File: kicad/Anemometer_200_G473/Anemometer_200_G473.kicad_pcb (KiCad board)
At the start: 2 copper layers, 23.3 x 37.9 mm, 81 parts, among them J1 Conn_01x01_Female, J10 Conn_01x01_Female, J11 USB_B_Micro, J12 Conn_01x01_Female, J13 Conn_01x01_Female, J14 Conn_01x01_Female, J15 Conn_01x01_Female, J16 Conn_01x01_Female, J17 Conn_01x01_Female, J18 Conn_01x01_Female, J2 Conn_01x01_Female, J20 Conn_01x01_Female, J21 Conn_01x01_Female, J22 Conn_01x01_Female, J3 Conn_01x08_Shielded, J9 Conn_01x01_Female, U1 W5500, U2 NCP1117-3.3, Y1 16, Y2 Crystal_GND24_Small

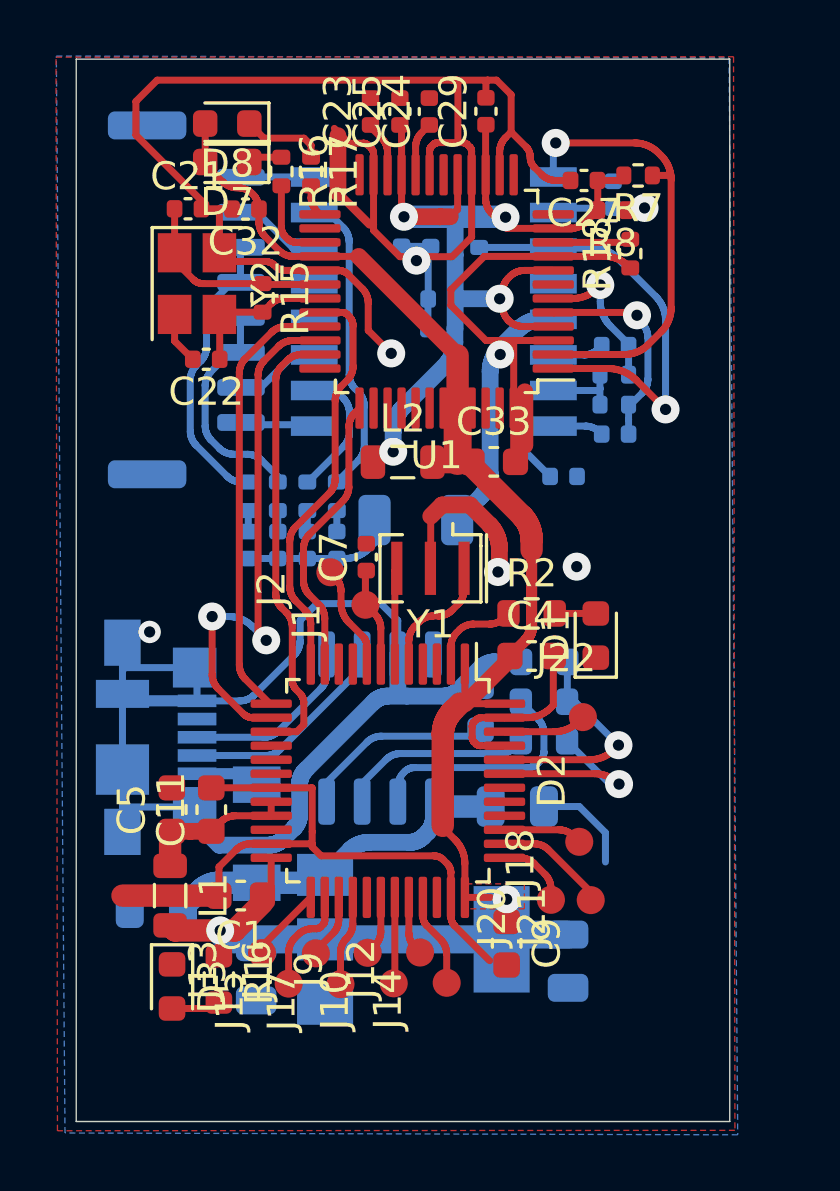
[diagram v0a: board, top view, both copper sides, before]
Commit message: изменено:      kicad/Anemometer_200_G473/Anemometer_200_G473-cache.lib 	изменено:      kicad/Anemometer_200_G473/Anemometer_200_G473.kicad_pcb 	изменено:      kicad/Anemometer_200_G473/Anemometer_200_G473.kicad_pcb-bak 	изменено:      kicad/Anemometer_200_G473/Anemometer_200_G473.sch 	изменено:      kicad/Anemometer_200_G473/Anemometer_200_G473.sch-bak 	изменено:      kicad/Anemometer_200_G473/sym-lib-table 	изменено:      stm32cubeide/Anemometer_G474CBT6_MATLAB/Anemometer_G473CBT7_MATLAB.ioc 	изменено:      stm32cubeide/Anemometer_G474CBT6_MATLAB/Core/Inc/main.h 	изменено:      stm32cubeide/Anemometer_G474CBT6_MATLAB/Core/Src/main.c 	изменено:      stm32cubeide/Anemometer_G474CBT6_MATLAB/Release/Anemometer_G473CBT7_MATLAB.elf 	изменено:      stm32cubeide/Anemometer_G474CBT6_MATLAB/Release/Anemometer_G473CBT7_MATLAB.list 	изменено:      stm32cubeide/Anemometer_G474CBT6_MATLAB/Release/Anemometer_G473CBT7_MATLAB.map 	изменено:      stm32cubeide/Anemometer_G474CBT6_MATLAB/Release/Core/Src/main.cyclo 	изменено:      stm32cubeide/Anemometer_G474CBT6_MATLAB/Release/Core/Src/main.o 	изменено:      stm32cubeide/Anemometer_G474CBT6_MATLAB/Release/Core/Src/main.su
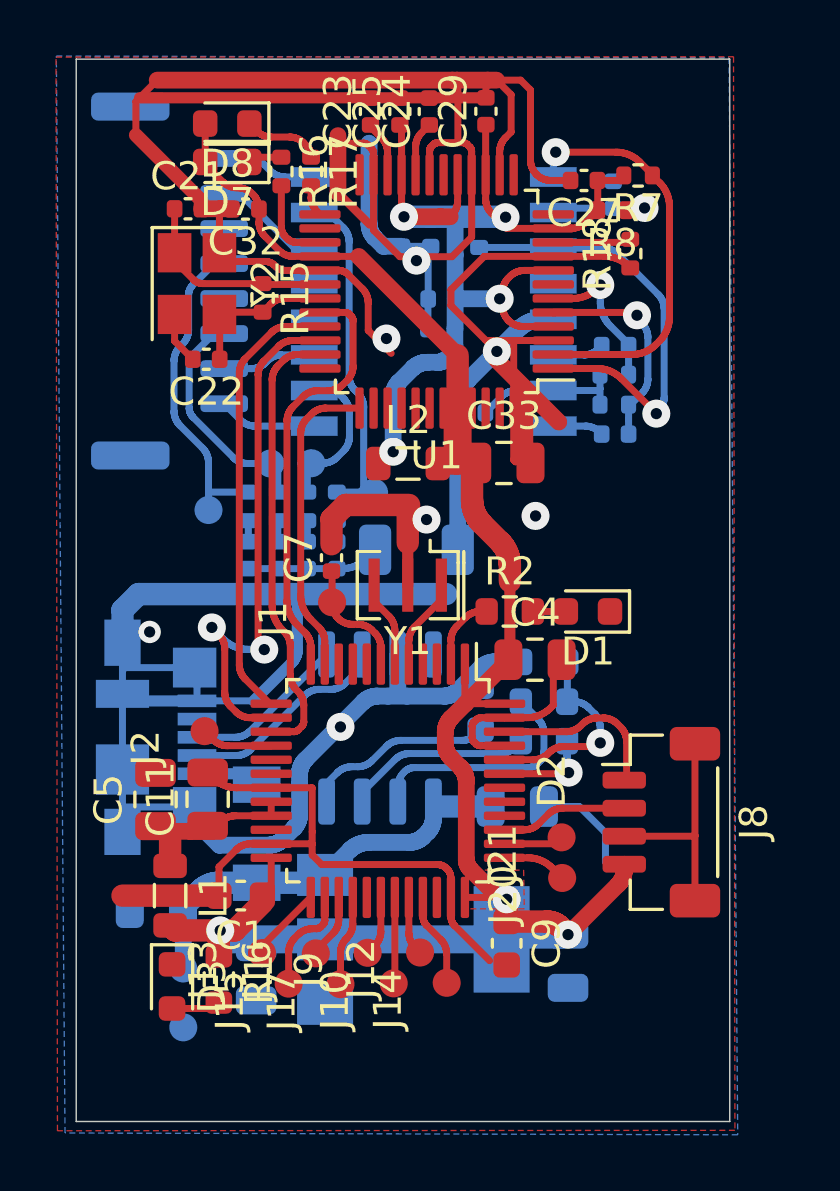
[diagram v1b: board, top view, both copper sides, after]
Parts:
- removed J22: Conn_01x01_Female, My-library:mini_conn
- added J19: Conn_01x01_Female, My-library:mini_conn, B.Cu at (21.0, 64.7)
- added J4: Conn_01x01_Female, My-library:mini_conn, B.Cu at (25.6, 44.6)
- added J5: Conn_01x01_Female, My-library:mini_conn, B.Cu at (27.8, 45.6)
- added J6: Conn_01x01_Female, My-library:mini_conn, B.Cu at (21.9, 46.2)
- added J7: Conn_01x01_Female, My-library:mini_conn, B.Cu at (24.1, 44.6)
- added J8: Conn_01x04_Shielded, Connector_JST:JST_SH_BM04B-SRSS-TB_1x04-1MP_P1.00mm_Vertical, F.Cu at (38.1, 57.4)
- C11, C33, C4, C5: footprint Capacitor_SMD:C_0603_1608Metric -> Capacitor_SMD:C_0805_2012Metric
- J18: moved to B.Cu
- moved J18 14.8 mm to (21.0, 62.6), turned to 0 degrees
- moved J2 7.23 mm to (21.8, 54.1)
- moved C19 3.98 mm to (31.3, 42.8), turned to 180 degrees
- moved J21 2.47 mm to (34.5, 57.9)
- moved C7 1.24 mm to (26.3, 48.0)
- moved J1 1.19 mm to (26.3, 49.5)
- moved C20 1.06 mm to (29.3, 47.7)
- moved Y1 1.01 mm to (29.0, 48.9)
- moved D1 0.90 mm to (35.5, 49.9), turned to 180 degrees
- moved J3 0.90 mm to (20.5, 38.1)
- moved J20 0.88 mm to (34.5, 59.4)
- moved R2 0.78 mm to (32.7, 49.9)
- moved C5 0.68 mm to (20.0, 56.6)
- moved C11 0.39 mm to (21.9, 56.6)
- moved C33 0.36 mm to (32.5, 44.6)
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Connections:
- net Net-(D6-Pad10) renamed /V1
- net Net-(D6-Pad15) renamed /V2
- net Net-(J3-Pad3) renamed /V3
- net Net-(J3-Pad5) renamed /V4
- C10 pad 1: Net-(C10-Pad1) -> /+5v
- C12 pad 1: Net-(C10-Pad1) -> /+5v
- D2 pad 16: (no net) -> /AIn
- D2 pad 39: /scl -> scl
- D2 pad 46: /sda -> sda
- D2 pad 8: /AIn -> (no net)
- D4 pad 1: Net-(C10-Pad1) -> /+5v
- D5 pad 5: Net-(C10-Pad1) -> /+5v
- J18 pad 1: /scl -> /+5v
- U2 pad 3: Net-(C10-Pad1) -> /+5v
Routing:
- net GND: track 173.5 -> 215.5 mm, vias 6 -> 7
- net /+5v: track 0.00 -> 15.2 mm
- net Net-(C10-Pad1): track 13.0 -> 0.00 mm
- net sda: track 0.00 -> 6.37 mm
- net +3V3: track 62.1 -> 66.9 mm, vias 2 -> 3
- net scl: track 0.00 -> 4.53 mm
- net /sda: track 2.96 -> 0.00 mm
- net /scl: track 2.81 -> 0.00 mm
- net Net-(D2-Pad43): track 6.68 -> 3.98 mm
- net /V3: track 10.3 -> 12.8 mm
- net /swc: track 4.05 -> 2.13 mm
- net Net-(C19-Pad1): track 7.32 -> 5.49 mm
- net Net-(D6-Pad1): track 16.4 -> 14.8 mm
- net /V2: track 10.9 -> 12.3 mm
- net /V4: track 8.18 -> 9.52 mm
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
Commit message: изменено:      kicad/Anemometer_200_G473/Anemometer_200_G473-cache.lib 	изменено:      kicad/Anemometer_200_G473/Anemometer_200_G473.kicad_pcb 	изменено:      kicad/Anemometer_200_G473/Anemometer_200_G473.kicad_pcb-bak 	изменено:      kicad/Anemometer_200_G473/Anemometer_200_G473.sch 	изменено:      kicad/Anemometer_200_G473/Anemometer_200_G473.sch-bak
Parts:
- moved R5 4.34 mm to (33.9, 56.0)
- moved C8 2.80 mm to (33.9, 51.7), turned to 0 degrees
- moved R4 1.57 mm to (33.9, 54.7)
- moved C12 1.54 mm to (33.8, 58.1)
- moved R3 1.28 mm to (33.9, 53.2)
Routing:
- net GND: track 215.5 -> 209.7 mm
- net Net-(D2-Pad44): track 7.37 -> 3.64 mm
- net Net-(C8-Pad1): track 6.82 -> 9.87 mm
- net Net-(D5-Pad6): track 8.55 -> 5.62 mm
- net Net-(D2-Pad43): track 3.98 -> 6.72 mm
- net /+5v: track 15.2 -> 16.4 mm
- net Net-(D5-Pad7): track 6.68 -> 7.89 mm

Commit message: изменено:      kicad/Anemometer_200_G473/Anemometer_200_G473.kicad_pcb 	изменено:      kicad/Anemometer_200_G473/Anemometer_200_G473.kicad_sch
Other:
- net class Default removed

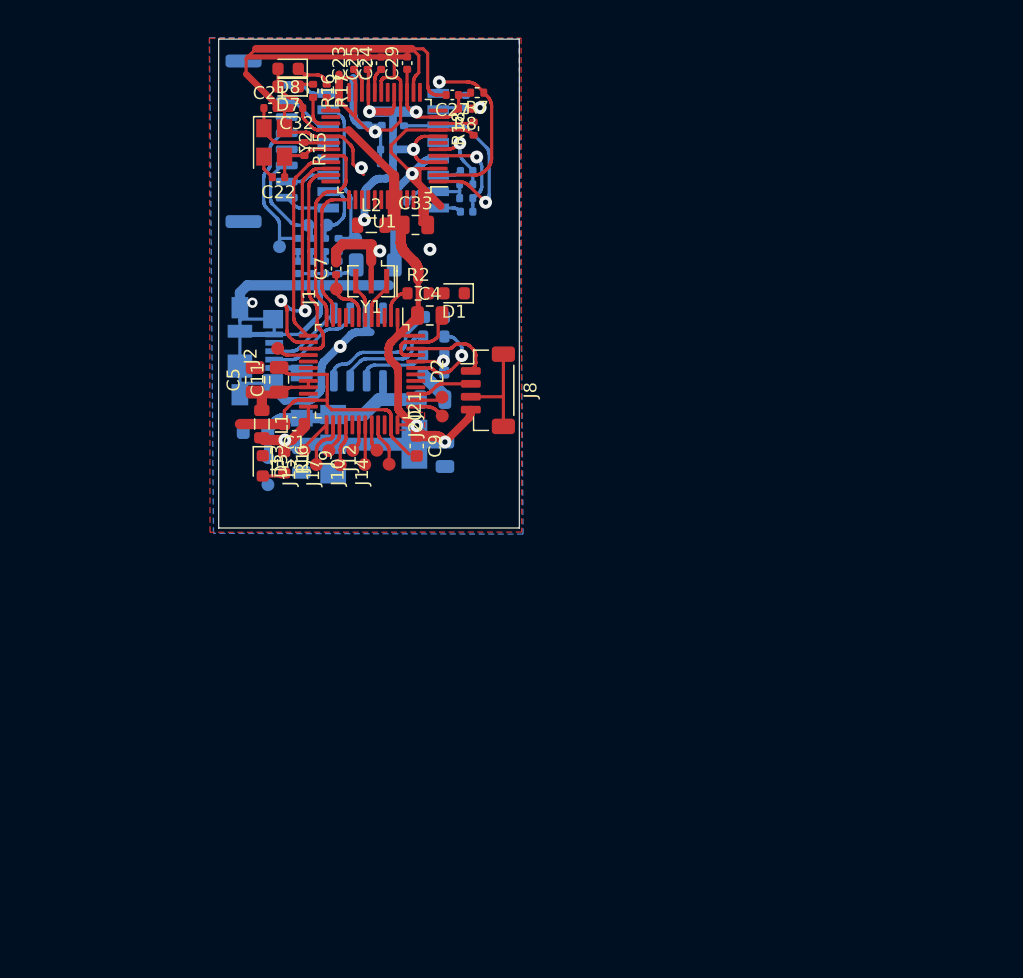
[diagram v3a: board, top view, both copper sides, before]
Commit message: изменено:      kicad/Amp200_2/Amp200-rescue.lib 	изменено:      kicad/Anemometer_200_G473/Anemometer_200_G473.kicad_pcb 	изменено:      kicad/Anemometer_200_G473/Anemometer_200_G473.kicad_prl 	изменено:      kicad/Anemometer_200_G473/Anemometer_200_G473.kicad_sch 	изменено:      kicad/Anemometer_200_G473/fp-info-cache 	изменено:      kicad/Anemometr_v3/Anemometr-rescue.lib
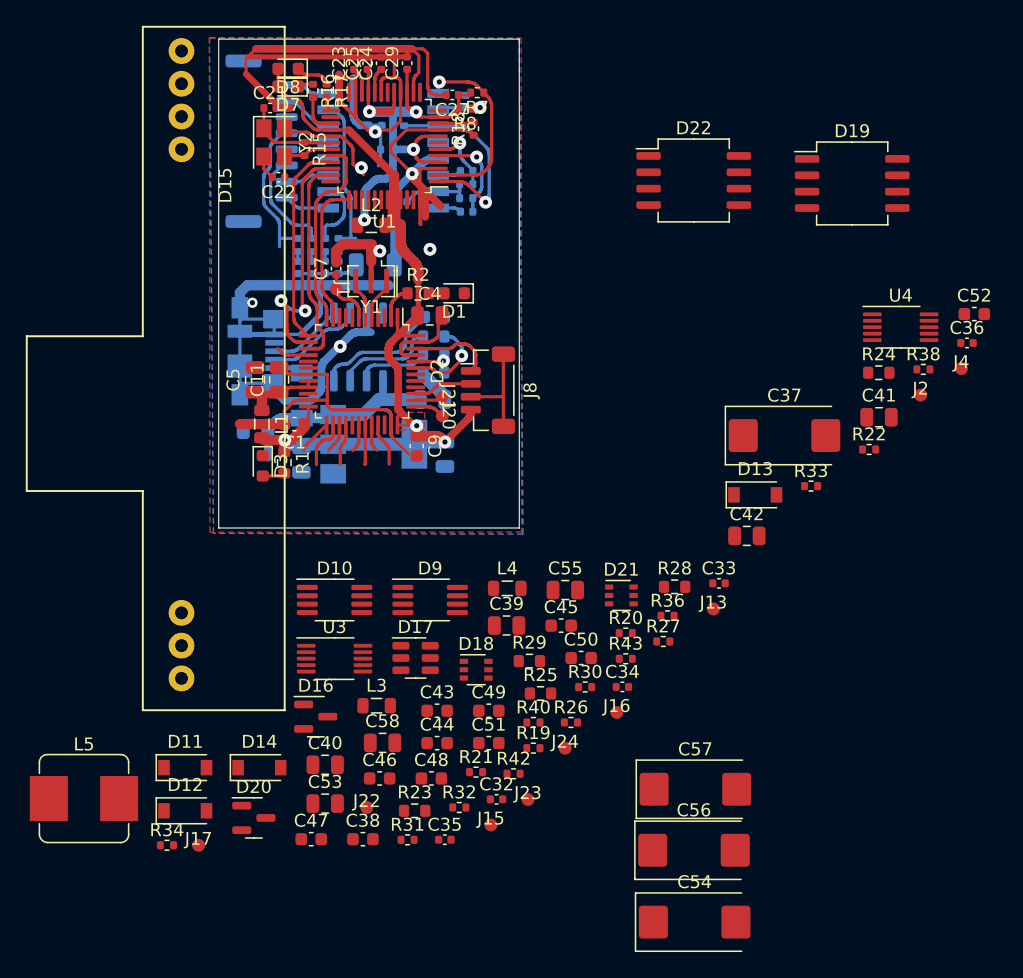
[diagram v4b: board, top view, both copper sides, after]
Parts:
- removed J10, J12, J14, J18, J19, J5, J6, J7, J9: Conn_01x01_Female, My-library:mini_conn
- added C34: 4.7u, Capacitor_SMD:C_0402_1005Metric, F.Cu at (48.5, 80.4)
- added C35: 4.7u, Capacitor_SMD:C_0402_1005Metric, F.Cu at (34.7, 92.2)
- added C36: 6.8n, Capacitor_SMD:C_0402_1005Metric, F.Cu at (75.2, 53.7)
- added C37: CP, Capacitor_Tantalum_SMD:CP_EIA-7343-40_Kemet-Y_Pad2.25x2.55mm_HandSolder, F.Cu at (61.1, 60.9)
- added C38: C, Capacitor_SMD:C_0603_1608Metric, F.Cu at (28.4, 92.2)
- added C39: C, Capacitor_SMD:C_0805_2012Metric, F.Cu at (39.5, 75.6)
- added C40: C, Capacitor_SMD:C_0805_2012Metric, F.Cu at (25.5, 86.4)
- added C41: C, Capacitor_SMD:C_0805_2012Metric, F.Cu at (68.4, 59.5)
- added C42: C, Capacitor_SMD:C_0805_2012Metric, F.Cu at (58.2, 68.7)
- added C43: C, Capacitor_SMD:C_0603_1608Metric, F.Cu at (34.1, 82.2)
- added C44: C, Capacitor_SMD:C_0603_1608Metric, F.Cu at (34.1, 84.8)
- added C45: C, Capacitor_SMD:C_0603_1608Metric, F.Cu at (43.8, 75.6)
- added C46: C, Capacitor_SMD:C_0603_1608Metric, F.Cu at (29.7, 87.5)
- added C47: C, Capacitor_SMD:C_0603_1608Metric, F.Cu at (24.4, 92.2)
- added C48: 85n, Capacitor_SMD:C_0603_1608Metric, F.Cu at (33.7, 87.5)
- added C49: 85n, Capacitor_SMD:C_0603_1608Metric, F.Cu at (38.1, 82.2)
- added C50: 85n, Capacitor_SMD:C_0603_1608Metric, F.Cu at (45.3, 78.2)
- added C51: 85n, Capacitor_SMD:C_0603_1608Metric, F.Cu at (38.1, 84.8)
- added C52: 85n, Capacitor_SMD:C_0603_1608Metric, F.Cu at (75.8, 51.5)
- added C53: C, Capacitor_SMD:C_0805_2012Metric, F.Cu at (25.5, 89.4)
- added C54: CP, Capacitor_Tantalum_SMD:CP_EIA-7343-40_Kemet-Y_Pad2.25x2.55mm_HandSolder, F.Cu at (54.1, 98.6)
- added C55: C, Capacitor_SMD:C_0805_2012Metric, F.Cu at (44.1, 72.9)
- added C56: CP, Capacitor_Tantalum_SMD:CP_EIA-7343-40_Kemet-Y_Pad2.25x2.55mm_HandSolder, F.Cu at (54.1, 93.1)
- added C57: CP, Capacitor_Tantalum_SMD:CP_EIA-7343-40_Kemet-Y_Pad2.25x2.55mm_HandSolder, F.Cu at (54.2, 88.3)
- added C58: C, Capacitor_SMD:C_0805_2012Metric, F.Cu at (29.9, 84.7)
- added D10: AD5245, Package_SO:MSOP-8_3x3mm_P0.65mm, F.Cu at (26.2, 73.7)
- added D11: D_Zener_Small, Diode_SMD:D_SOD-123, F.Cu at (14.6, 86.7)
- added D12: D_Zener_Small, Diode_SMD:D_SOD-123, F.Cu at (14.6, 90.0)
- added D13: D_Zener_Small, Diode_SMD:D_SOD-123, F.Cu at (58.8, 65.5)
- added D14: D_Zener_Small, Diode_SMD:D_SOD-123, F.Cu at (20.4, 86.7)
- added D15: RT9400, lib:TR9400, F.Cu at (14.3, 41.2)
- added D16: BAT54C, Package_TO_SOT_SMD:SOT-23, F.Cu at (24.7, 82.7)
- added D17: LMR50410, Package_TO_SOT_SMD:SOT-23-6, F.Cu at (32.5, 78.2)
- added D18: DMN5L06DWK-7, Package_TO_SOT_SMD:SOT-363_SC-70-6, F.Cu at (37.2, 79.1)
- added D19: DMHC3025LSD, Package_SO:SO-8_5.3x6.2mm_P1.27mm, F.Cu at (66.3, 41.4)
- added D20: BAT54C, Package_TO_SOT_SMD:SOT-23, F.Cu at (19.9, 90.5)
- added D21: DMN5L06DWK-7, Package_TO_SOT_SMD:SOT-363_SC-70-6, F.Cu at (48.4, 73.3)
- added D22: DMHC3025LSD, Package_SO:SO-8_5.3x6.2mm_P1.27mm, F.Cu at (54.0, 41.1)
- added D9: MAX4477, Package_SO:MSOP-8_3x3mm_P0.65mm, F.Cu at (33.6, 73.7)
- added J22: Conn_01x01_Female, lib:conn_mini, F.Cu at (28.7, 89.7)
- added J23: Conn_01x01_Female, lib:conn_mini, F.Cu at (41.2, 89.1)
- added J24: Conn_01x01_Female, lib:conn_mini, F.Cu at (44.1, 85.1)
- added L3: 47u, Inductor_SMD:L_0805_2012Metric, F.Cu at (29.4, 81.8)
- added L4: 10u, Inductor_SMD:L_0805_2012Metric, F.Cu at (39.6, 72.8)
- added L5: 10u, Inductor_SMD:L_Bourns_SRP7028A_7.3x6.6mm, F.Cu at (6.76, 89.0)
- added R19: 100k, Resistor_SMD:R_0402_1005Metric, F.Cu at (41.6, 85.1)
- added R20: 100k, Resistor_SMD:R_0402_1005Metric, F.Cu at (48.8, 76.2)
- added R21: 100k, Resistor_SMD:R_0402_1005Metric, F.Cu at (37.2, 87.0)
- added R22: 100k, Resistor_SMD:R_0402_1005Metric, F.Cu at (67.6, 62.0)
- added R23: R, Resistor_SMD:R_0603_1608Metric, F.Cu at (32.4, 90.0)
- added R24: R, Resistor_SMD:R_0603_1608Metric, F.Cu at (68.4, 56.0)
- added R25: R, Resistor_SMD:R_0603_1608Metric, F.Cu at (42.2, 80.9)
- added R26: 12.4k, Resistor_SMD:R_0402_1005Metric, F.Cu at (44.5, 83.2)
- added R27: 12.4k, Resistor_SMD:R_0402_1005Metric, F.Cu at (51.7, 76.9)
- added R28: R, Resistor_SMD:R_0603_1608Metric, F.Cu at (52.6, 72.6)
- added R29: R, Resistor_SMD:R_0603_1608Metric, F.Cu at (41.3, 78.4)
- added R30: 100, Resistor_SMD:R_0402_1005Metric, F.Cu at (45.6, 80.4)
- added R31: 100, Resistor_SMD:R_0402_1005Metric, F.Cu at (31.9, 92.2)
- added R32: 100, Resistor_SMD:R_0402_1005Metric, F.Cu at (35.9, 89.7)
- added R33: 100, Resistor_SMD:R_0402_1005Metric, F.Cu at (63.1, 64.8)
- added R34: 12.4k, Resistor_SMD:R_0402_1005Metric, F.Cu at (13.2, 92.7)
- added R36: 12.4k, Resistor_SMD:R_0402_1005Metric, F.Cu at (52.0, 74.9)
- added R38: 12.4k, Resistor_SMD:R_0402_1005Metric, F.Cu at (71.8, 55.8)
- added R40: 12.4k, Resistor_SMD:R_0402_1005Metric, F.Cu at (41.6, 83.2)
- added R42: 12.4k, Resistor_SMD:R_0402_1005Metric, F.Cu at (40.1, 87.1)
- added R43: 12.4k, Resistor_SMD:R_0402_1005Metric, F.Cu at (48.8, 78.2)
- added U3: TS5A23159DGS, Package_SO:VSSOP-10_3x3mm_P0.5mm, F.Cu at (26.2, 78.2)
- added U4: TS5A23159DGS, Package_SO:VSSOP-10_3x3mm_P0.5mm, F.Cu at (70.1, 52.5)
- C33: footprint Capacitor_SMD:C_0805_2012Metric -> Capacitor_SMD:C_0402_1005Metric
- D7: value green -> red
- D8: value red -> green
- J1, J13, J15, J16, J17, J2, J20, J21: footprint My-library:mini_conn -> lib:conn_mini
- J4: footprint My-library:mini_conn -> lib:conn_mini; moved to F.Cu
- L2: value L -> 10u
- Y2: value Crystal_GND24_Small -> 25MHz
- moved C32 55.8 mm to (38.8, 89.1), turned to 0 degrees
- moved J4 50.4 mm to (74.8, 55.7)
- moved J2 50.0 mm to (71.6, 57.8), turned to 0 degrees
- moved C33 36.4 mm to (56.0, 72.4)
- moved J13 34.0 mm to (55.6, 74.3), turned to 0 degrees
- moved J17 31.5 mm to (15.6, 92.7), turned to 0 degrees
- moved J15 31.1 mm to (38.3, 91.1), turned to 0 degrees
- moved J16 30.2 mm to (48.1, 82.4), turned to 0 degrees
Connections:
- C10 pad 1: /+5v -> +5v
- C12 pad 1: /+5v -> +5v
- D2 pad 10: (no net) -> unconnected-(D2-Pad10)
- D2 pad 16: /AIn -> Analog
- D2 pad 17: (no net) -> unconnected-(D2-Pad17)
- D2 pad 18: (no net) -> unconnected-(D2-Pad18)
- D2 pad 22: (no net) -> unconnected-(D2-Pad22)
- D2 pad 25: /selZ1 -> selZ1
- D2 pad 26: /selZ2 -> selZ2
- D2 pad 27: /selZ3 -> selZ3
- D2 pad 28: /selZ4 -> selZ4
- D2 pad 29: (no net) -> unconnected-(D2-Pad29)
- D2 pad 3: (no net) -> unconnected-(D2-Pad3)
- D2 pad 30: /Z1 -> Z1
- D2 pad 31: /Z2 -> Z2
- D2 pad 32: /Z3 -> Z3
- D2 pad 33: /Z4 -> Z4
- D2 pad 34: (no net) -> unconnected-(D2-Pad34)
- D2 pad 4: (no net) -> unconnected-(D2-Pad4)
- D2 pad 40: (no net) -> unconnected-(D2-Pad40)
- D2 pad 41: (no net) -> unconnected-(D2-Pad41)
- D2 pad 42: (no net) -> unconnected-(D2-Pad42)
- D2 pad 8: (no net) -> unconnected-(D2-Pad8)
- D2 pad 9: (no net) -> unconnected-(D2-Pad9)
- D4 pad 1: /+5v -> +5v
- D5 pad 4: (no net) -> unconnected-(D5-Pad4)
- D5 pad 5: /+5v -> Net-(D4-Pad2)
- D6 pad 10: /V1 -> Net-(D15-Pad2)
- D6 pad 12: (no net) -> unconnected-(D6-Pad12)
- D6 pad 13: (no net) -> unconnected-(D6-Pad13)
- D6 pad 15: /V2 -> Net-(D15-Pad1)
- D6 pad 4: GND -> unconnected-(D6-Pad4)
- D6 pad 5: GND -> unconnected-(D6-Pad5)
- J11 pad 4: (no net) -> unconnected-(J11-Pad4)
- J13 pad 1: /selZ1 -> Net-(J13-Pad1)
- J15 pad 1: /selZ2 -> Net-(J15-Pad1)
- J16 pad 1: /selZ3 -> Net-(J16-Pad1)
- J17 pad 1: /selZ4 -> Net-(D11-Pad1)
- J2 pad 1: /AIn -> Net-(J2-Pad1)
- J3 pad 3: /V3 -> Net-(D15-Pad4)
- J3 pad 4: /V3 -> Net-(D15-Pad4)
- J3 pad 5: /V4 -> Net-(D15-Pad3)
- J3 pad 6: /V4 -> Net-(D15-Pad3)
- J4 pad 1: /V1 -> GND
- R10 pad 2: /V2 -> Net-(D15-Pad4)
- R11 pad 2: /V4 -> Net-(D15-Pad2)
- R12 pad 2: /V3 -> Net-(D15-Pad3)
- R9 pad 2: /V1 -> Net-(D15-Pad1)
- U1 pad 12: (no net) -> unconnected-(U1-Pad12)
- U1 pad 13: (no net) -> unconnected-(U1-Pad13)
- U1 pad 18: (no net) -> unconnected-(U1-Pad18)
- U1 pad 24: (no net) -> unconnected-(U1-Pad24)
- U1 pad 26: (no net) -> unconnected-(U1-Pad26)
- U1 pad 36: (no net) -> unconnected-(U1-Pad36)
- U1 pad 38: (no net) -> unconnected-(U1-Pad38)
- U1 pad 39: (no net) -> unconnected-(U1-Pad39)
- U1 pad 40: (no net) -> unconnected-(U1-Pad40)
- U1 pad 41: (no net) -> unconnected-(U1-Pad41)
- U1 pad 42: (no net) -> unconnected-(U1-Pad42)
- U1 pad 46: (no net) -> unconnected-(U1-Pad46)
- U1 pad 47: (no net) -> unconnected-(U1-Pad47)
- U1 pad 7: (no net) -> unconnected-(U1-Pad7)
- U2 pad 3: /+5v -> +5v
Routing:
- net Net-(D15-Pad4): track 0.00 -> 25.1 mm
- net /+5v: track 16.4 -> 0.00 mm
- net +5v: track 0.00 -> 16.4 mm
- net /V3: track 12.8 -> 0.00 mm
- net /V2: track 12.3 -> 0.00 mm
- net Net-(D15-Pad3): track 0.00 -> 9.52 mm
- net /V4: track 9.52 -> 0.00 mm
- net Net-(D15-Pad2): track 0.00 -> 5.53 mm
- net /V1: track 5.53 -> 0.00 mm
- net selZ2: track 0.00 -> 3.84 mm
- net /selZ2: track 3.84 -> 0.00 mm
- net Z4: track 0.00 -> 3.35 mm
- net /Z4: track 3.35 -> 0.00 mm
- net selZ4: track 0.00 -> 3.22 mm
- net /selZ4: track 3.22 -> 0.00 mm
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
